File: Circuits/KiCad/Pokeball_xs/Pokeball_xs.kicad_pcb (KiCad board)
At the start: 2 copper layers, 30 x 30 mm, 21 parts, among them J1 Conn_01x05, J2 Conn_01x02, J3 Conn_01x06, U1 PIC12LF1571T-I_SN, U2 MCP1754ST-3302E_DB

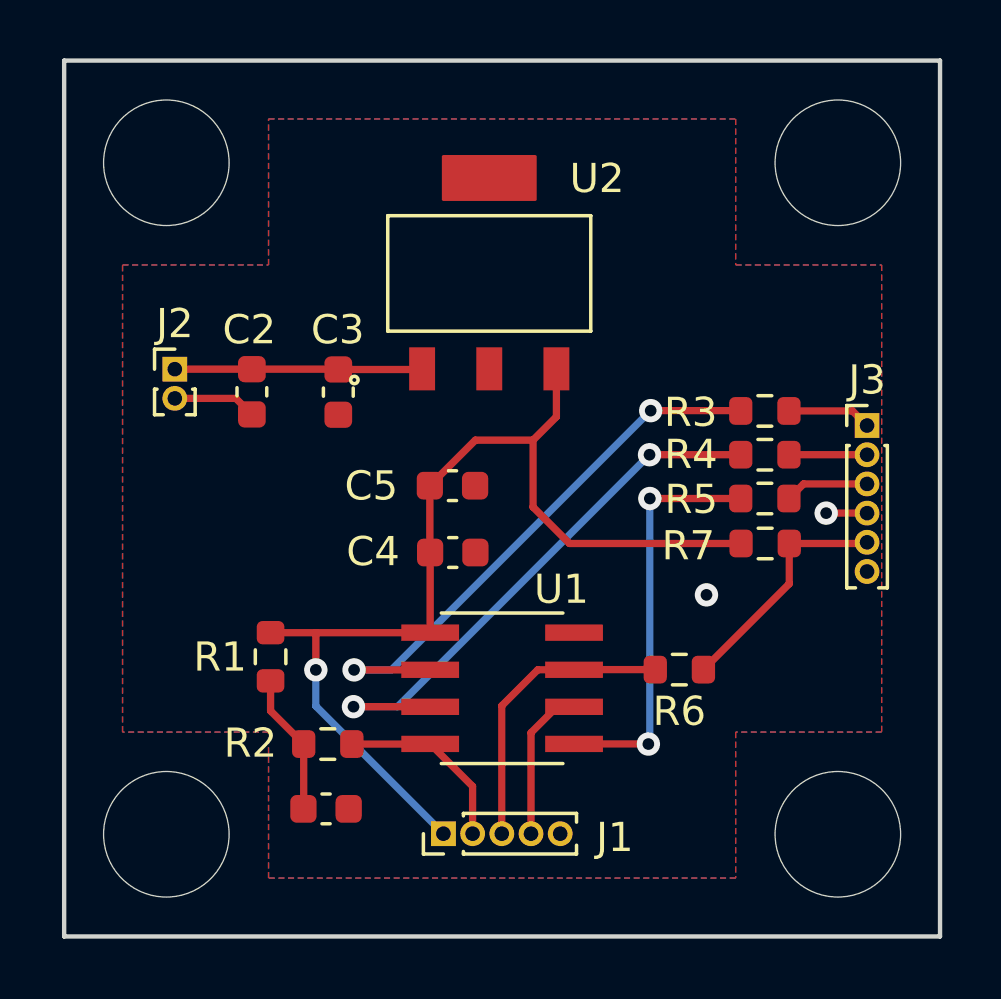
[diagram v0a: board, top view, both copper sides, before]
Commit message: v 0.0.0.1 - Include the charging circuit on the PCB
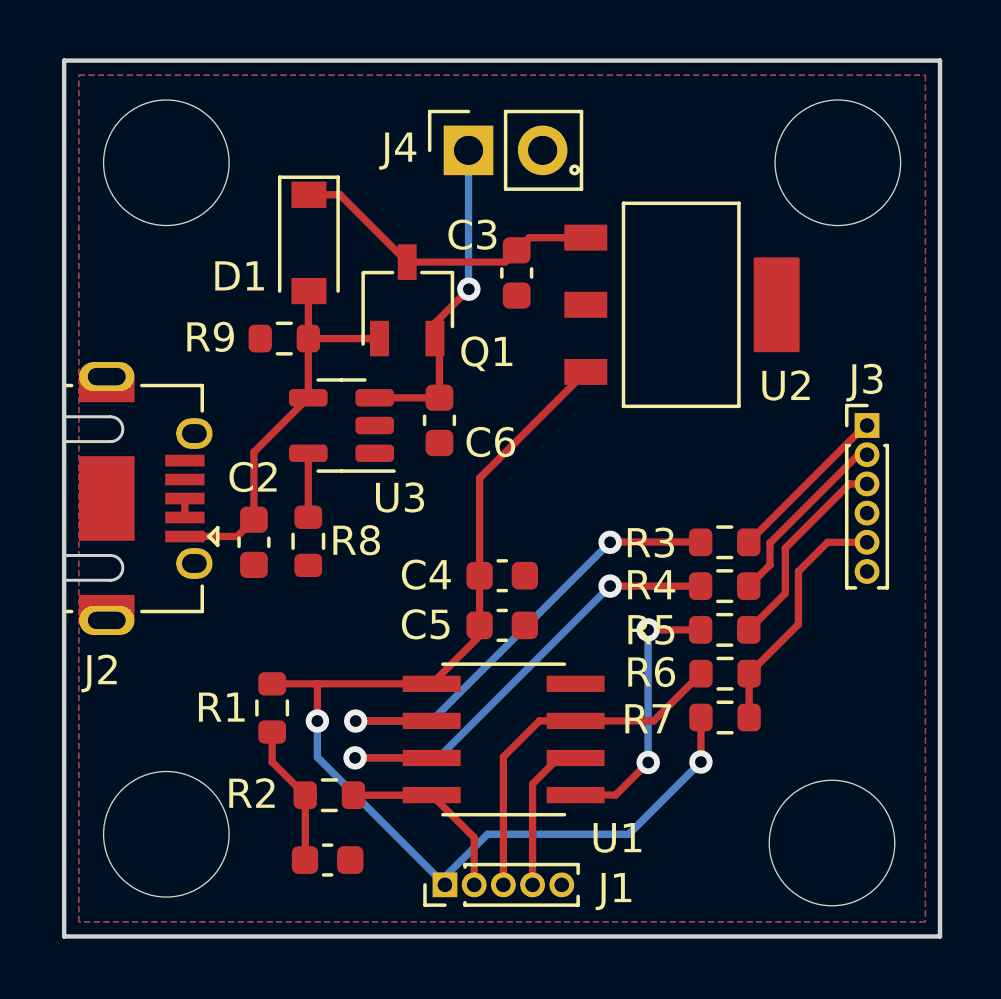
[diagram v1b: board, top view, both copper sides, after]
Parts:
- added C6: 4.7uF, Capacitor_SMD:C_0603_1608Metric, F.Cu at (137.9, 90.8)
- added D1: 40V 500mA, Diode_SMD:D_SOD-123, F.Cu at (133.4, 84.7)
- added J4: Battery, Connector_PinSocket_2.54mm:PinSocket_1x02_P2.54mm_Vertical, F.Cu at (138.8, 81.6)
- added Q1: 60V 170mA, Package_TO_SOT_SMD:TSOT-23, F.Cu at (136.7, 86.7)
- added R8: 10k, Resistor_SMD:R_0603_1608Metric, F.Cu at (133.4, 95.0)
- added R9: 10k, Resistor_SMD:R_0603_1608Metric, F.Cu at (132.5, 88.0)
- added U3: MCP73831-2-OT, Package_TO_SOT_SMD:SOT-23-5, F.Cu at (134.5, 91.0)
- C2: value 10uF 10v -> 4.7uF
- J2: value Conn_01x02 -> USB_B_Micro; footprint Connector_PinHeader_1.00mm:PinHeader_1x02_P1.00mm_Vertical -> Connector_USB:USB_Micro-AB_Molex_47590-0001
- moved C3 7.35 mm to (140.5, 85.8)
- moved U2 6.66 mm to (146.1, 86.9), turned to -90 degrees
- moved R7 6.12 mm to (147.6, 101.0)
- moved C2 5.16 mm to (131.5, 95.0)
- moved C5 5.08 mm to (140.0, 97.8)
- moved J2 5.01 mm to (126.5, 93.5), turned to -90 degrees
- moved R3 4.71 mm to (147.6, 95.0)
- moved R4 4.71 mm to (147.6, 96.5)
- moved R5 4.71 mm to (147.6, 98.0)
- moved C4 1.87 mm to (140.0, 96.1)
- moved C1 1.75 mm to (134.0, 105.9)
- moved J1 1.75 mm to (138.0, 106.7)
- moved R1 1.75 mm to (132.1, 100.7)
- moved R2 1.75 mm to (134.1, 103.7)
- moved U1 1.75 mm to (140.1, 101.8)
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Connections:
- C3 pad 1: Net-(C2-Pad1) -> Net-(C3-Pad1)
- J2 pad 2: GND -> Net-(J2-Pad2)
- U2 pad 1: Net-(C2-Pad1) -> Net-(C3-Pad1)
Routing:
- net Net-(C6-Pad1): track 0.00 -> 11.2 mm, vias 0 -> 1
- net Net-(C3-Pad1): track 0.00 -> 10.8 mm
- net Net-(C2-Pad1): track 8.48 -> 13.6 mm
- net PWM_3_BLUE: track 14.1 -> 9.29 mm
- net GND: track 4.27 -> 0.00 mm, vias 2 -> 0
- net Net-(J3-Pad3): track 2.88 -> 7.03 mm
- net Net-(J3-Pad2): track 2.68 -> 6.35 mm
- net Vcc: track 36.1 -> 39.2 mm, vias 1 -> 2
- net Net-(J3-Pad1): track 2.88 -> 5.71 mm
- net PWM_1_RED: track 19.5 -> 17.0 mm
- net PWM_2_GREEN: track 19.5 -> 16.9 mm
- net Net-(R8-Pad1): track 0.00 -> 2.19 mm
- net PGD: track 10.1 -> 12.3 mm
- net Net-(J2-Pad2): track 0.00 -> 0.65 mm

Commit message: v 0.0.0.2 - Testing the pwm output on the switch. Creation of the README.md.
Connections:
- net PWM_1_RED renamed PWM_4_RED
- net PWM_2_GREEN renamed PWM_3_GREEN
- net PWM_3_BLUE renamed PWM_1_BLUE
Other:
- outline, holes or cut-outs redrawn
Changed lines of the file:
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@@
   (net 6 "PGD")
   (net 7 "Net-(C2-Pad1)")
-  (net 8 "PWM_3_BLUE")
+  (net 8 "PWM_4_RED")
   (net 9 "Net-(J3-Pad1)")
-  (net 10 "PWM_2_GREEN")
+  (net 10 "PWM_3_GREEN")
   (net 11 "Net-(J3-Pad2)")
-  (net 12 "PWM_1_RED")
+  (net 12 "PWM_1_BLUE")
   (net 13 "Net-(J3-Pad3)")
   (net 14 "Net-(J3-Pad5)")
@@
       (net 4 "Vcc") (pinfunction "VDD") (pintype "power_in"))
     (pad "2" smd rect locked (at -2.4638 -0.635) (size 1.9812 0.5588) (layers "F.Cu" "F.Paste" "F.Mask")
-      (net 12 "PWM_1_RED") (pinfunction "RA5") (pintype "bidirectional"))
+      (net 8 "PWM_4_RED") (pinfunction "RA5") (pintype "bidirectional"))
     (pad "3" smd rect locked (at -2.4638 0.635) (size 1.9812 0.5588) (layers "F.Cu" "F.Paste" "F.Mask")
-      (net 10 "PWM_2_GREEN") (pinfunction "RA4") (pintype "bidirectional"))
+      (net 10 "PWM_3_GREEN") (pinfunction "RA4") (pintype "bidirectional"))
     (pad "4" smd rect locked (at -2.4638 1.905) (size 1.9812 0.5588) (layers "F.Cu" "F.Paste" "F.Mask")
       (net 1 "MCLR") (pinfunction "RA3/*MCLR/VPP") (pintype "bidirectional"))
     (pad "5" smd rect locked (at 2.4638 1.905) (size 1.9812 0.5588) (layers "F.Cu" "F.Paste" "F.Mask")
-      (net 8 "PWM_3_BLUE") (pinfunction "RA2") (pintype "bidirectional"))
+      (net 12 "PWM_1_BLUE") (pinfunction "RA2") (pintype "bidirectional"))
     (pad "6" smd rect locked (at 2.4638 0.635) (size 1.9812 0.5588) (layers "F.Cu" "F.Paste" "F.Mask")
       (net 5 "PGC") (pinfunction "RA1/ICSPCLK") (pintype "bidirectional"))
@@
       (net 9 "Net-(J3-Pad1)") (pintype "passive"))
     (pad "2" smd roundrect locked (at 0.825 0 180) (size 0.8 0.95) (layers "F.Cu" "F.Paste" "F.Mask") (roundrect_rratio 0.25)
-      (net 12 "PWM_1_RED") (pintype "passive"))
+      (net 8 "PWM_4_RED") (pintype "passive"))
     (model "${KISYS3DMOD}/Resistor_SMD.3dshapes/R_0603_1608Metric.wrl"
       (offset (xyz 0 0 0))
@@
       (net 11 "Net-(J3-Pad2)") (pintype "passive"))
     (pad "2" smd roundrect locked (at 0.825 0 180) (size 0.8 0.95) (layers "F.Cu" "F.Paste" "F.Mask") (roundrect_rratio 0.25)
-      (net 10 "PWM_2_GREEN") (pintype "passive"))
+      (net 10 "PWM_3_GREEN") (pintype "passive"))
     (model "${KISYS3DMOD}/Resistor_SMD.3dshapes/R_0603_1608Metric.wrl"
       (offset (xyz 0 0 0))
@@
       (net 13 "Net-(J3-Pad3)") (pintype "passive"))
     (pad "2" smd roundrect locked (at 0.825 0 180) (size 0.8 0.95) (layers "F.Cu" "F.Paste" "F.Mask") (roundrect_rratio 0.25)
-      (net 8 "PWM_3_BLUE") (pintype "passive"))
+      (net 12 "PWM_1_BLUE") (pintype "passive"))
     (model "${KISYS3DMOD}/Resistor_SMD.3dshapes/R_0603_1608Metric.wrl"
       (offset (xyz 0 0 0))
@@
   (gr_line (start 140 78.5) (end 140 108.5) (layer "Dwgs.User") (width 0.15))
   (gr_line (start 125 93.5) (end 155 93.5) (layer "Dwgs.User") (width 0.15))
-  (gr_line (start 125 78.5) (end 125 108.5) (layer "Edge.Cuts") (width 0.15))
+  (gr_line (start 125.01 89.75) (end 125 78.5) (layer "Edge.Cuts") (width 0.05))
+  (gr_line (start 125.01 97.25) (end 125 108.5) (layer "Edge.Cuts") (width 0.05))
   (gr_line (start 155 78.5) (end 125 78.5) (layer "Edge.Cuts") (width 0.15))
   (gr_line (start 155 108.5) (end 155 78.5) (layer "Edge.Cuts") (width 0.15))
@@
   (segment (start 131.5 91.9125) (end 133.3625 90.05) (width 0.25) (layer "F.Cu") (net 7))
   (segment (start 135.799229 88.021012) (end 135.79957 88.021353) (width 0.25) (layer "F.Cu") (net 7))
-  (segment (start 145.006003 102.540308) (end 143.888811 103.6575) (width 0.25) (layer "F.Cu") (net 8))
-  (segment (start 143.888811 103.6575) (end 142.5178 103.6575) (width 0.25) (layer "F.Cu") (net 8))
-  (segment (start 145 98) (end 146.8 98) (width 0.25) (layer "F.Cu") (net 8))
-  (via (at 145.006003 102.540308) (size 0.8) (drill 0.4) (layers "F.Cu" "B.Cu") (free) (net 8))
-  (via (at 145 98) (size 0.8) (drill 0.4) (layers "F.Cu" "B.Cu") (net 8))
-  (segment (start 145 102.534305) (end 145 98) (width 0.25) (layer "B.Cu") (net 8))
-  (segment (start 145.006003 102.540308) (end 145 102.534305) (width 0.25) (layer "B.Cu") (net 8))
+  (segment (start 143.71 94.99) (end 146.79 94.99) (width 0.25) (layer "F.Cu") (net 8))
+  (segment (start 134.984 101.1225) (end 137.5852 101.1225) (width 0.25) (layer "F.Cu") (net 8))
+  (segment (start 146.79 94.99) (end 146.8 95) (width 0.25) (layer "F.Cu") (net 8))
+  (segment (start 143.7 95) (end 143.71 94.99) (width 0.25) (layer "F.Cu") (net 8))
+  (segment (start 137.5852 101.1225) (end 137.5902 101.1175) (width 0.25) (layer "F.Cu") (net 8))
+  (via (at 143.7 95) (size 0.8) (drill 0.4) (layers "F.Cu" "B.Cu") (net 8))
+  (via (at 134.984 101.1225) (size 0.8) (drill 0.4) (layers "F.Cu" "B.Cu") (net 8))
+  (segment (start 134.984 101.1225) (end 137.5775 101.1225) (width 0.25) (layer "B.Cu") (net 8))
+  (segment (start 137.5775 101.1225) (end 143.7 95) (width 0.25) (layer "B.Cu") (net 8))
   (segment (start 148.45 94.99003) (end 152.44003 91) (width 0.25) (layer "F.Cu") (net 9))
   (segment (start 148.45 95) (end 148.45 94.99003) (width 0.25) (layer "F.Cu") (net 9))
@@
   (segment (start 152.2 92) (end 152.5 92) (width 0.25) (layer "F.Cu") (net 11))
   (segment (start 149.17452 95.77548) (end 149.17452 95.02548) (width 0.25) (layer "F.Cu") (net 11))
-  (segment (start 143.71 94.99) (end 146.79 94.99) (width 0.25) (layer "F.Cu") (net 12))
-  (segment (start 134.984 101.1225) (end 137.5852 101.1225) (width 0.25) (layer "F.Cu") (net 12))
-  (segment (start 146.79 94.99) (end 146.8 95) (width 0.25) (layer "F.Cu") (net 12))
-  (segment (start 143.7 95) (end 143.71 94.99) (width 0.25) (layer "F.Cu") (net 12))
-  (segment (start 137.5852 101.1225) (end 137.5902 101.1175) (width 0.25) (layer "F.Cu") (net 12))
-  (via (at 143.7 95) (size 0.8) (drill 0.4) (layers "F.Cu" "B.Cu") (net 12))
-  (via (at 134.984 101.1225) (size 0.8) (drill 0.4) (layers "F.Cu" "B.Cu") (net 12))
-  (segment (start 134.984 101.1225) (end 137.5775 101.1225) (width 0.25) (layer "B.Cu") (net 12))
-  (segment (start 137.5775 101.1225) (end 143.7 95) (width 0.25) (layer "B.Cu") (net 12))
+  (segment (start 145.006003 102.540308) (end 143.888811 103.6575) (width 0.25) (layer "F.Cu") (net 12))
+  (segment (start 143.888811 103.6575) (end 142.5178 103.6575) (width 0.25) (layer "F.Cu") (net 12))
+  (segment (start 145 98) (end 146.8 98) (width 0.25) (layer "F.Cu") (net 12))
+  (via (at 145.006003 102.540308) (size 0.8) (drill 0.4) (layers "F.Cu" "B.Cu") (free) (net 12))
+  (via (at 145 98) (size 0.8) (drill 0.4) (layers "F.Cu" "B.Cu") (net 12))
+  (segment (start 145 102.534305) (end 145 98) (width 0.25) (layer "B.Cu") (net 12))
+  (segment (start 145.006003 102.540308) (end 145 102.534305) (width 0.25) (layer "B.Cu") (net 12))
   (segment (start 149.7 95.2) (end 151.9 93) (width 0.25) (layer "F.Cu") (net 13))
   (segment (start 149.7 96.75) (end 149.7 95.2) (width 0.25) (layer "F.Cu") (net 13))
@@
     (connect_pads (clearance 0))
     (min_thickness 0.254)
-    (keepout (tracks not_allowed) (vias not_allowed) (pads not_allowed ) (copperpour not_allowed) (footprints allowed))
+    (keepout (tracks not_allowed) (vias not_allowed) (pads not_allowed) (copperpour not_allowed) (footprints allowed))
     (fill (thermal_gap 0.508) (thermal_bridge_width 0.508))
     (polygon
@@
     (connect_pads (clearance 0))
     (min_thickness 0.254)
-    (keepout (tracks not_allowed) (vias not_allowed) (pads not_allowed ) (copperpour not_allowed) (footprints allowed))
+    (keepout (tracks not_allowed) (vias not_allowed) (pads not_allowed) (copperpour not_allowed) (footprints allowed))
     (fill (thermal_gap 0.508) (thermal_bridge_width 0.508))
     (polygon

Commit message: v 0.0.0.3 - updates to the board and the mechanical system.
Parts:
- added G***: LOGO, Psyduck_xs:Psyduck_xs, F.Cu at (135.0, 81.0)
- moved R7 3.86 mm to (146.0, 104.5), turned to 90 degrees
- moved U2 1.30 mm to (145.0, 87.5)
- moved C3 1.00 mm to (139.5, 85.8)
- moved D1 0.67 mm to (134.0, 85.0)
- moved C1 0.61 mm to (134.5, 105.5)
- moved R2 0.54 mm to (134.5, 104.0)
- moved R1 0.51 mm to (132.5, 100.3)
- moved H3 0.36 mm to (151.5, 105.0)
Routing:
- net Vcc: track 39.2 -> 34.9 mm
- net Net-(J3-Pad5): track 8.52 -> 12.2 mm
- net Net-(C3-Pad1): track 10.8 -> 8.83 mm
- net Net-(C6-Pad1): track 11.2 -> 11.9 mm
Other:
- board text added: "+"
- board text added: "-"
- board text added: "B"
- board text added: "BTN"
- board text added: "G"
- board text added: "R"

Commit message: v 0.0.0.4 - submit rev 1 of the pokeball to pcbway.
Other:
- board text added: "JKnapp Rev1"
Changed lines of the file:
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@@
       (layerselection 0x00010fc_ffffffff)
       (disableapertmacros false)
-      (usegerberextensions false)
-      (usegerberattributes true)
+      (usegerberextensions true)
+      (usegerberattributes false)
       (usegerberadvancedattributes true)
-      (creategerberjobfile true)
+      (creategerberjobfile false)
       (svguseinch false)
       (svgprecision 6)
@@
       (outputformat 1)
       (mirror false)
-      (drillshape 1)
+      (drillshape 0)
       (scaleselection 1)
-      (outputdirectory "")
+      (outputdirectory "Pokeball_Kicad_Rev_1/")
     )
   )
@@
     (effects (font (size 0.5 0.5) (thickness 0.125)))
   )
+  (gr_text "JKnapp\nRev1" (at 144.5 81.5 90) (layer "F.SilkS")
+    (effects (font (size 0.5 0.5) (thickness 0.125)))
+  )

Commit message: v 0.0.0.8 - Board submitted to pcbway
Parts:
- removed R7: 4.7k, Resistor_SMD:R_0603_1608Metric
- added C7: 47uF, Capacitor_SMD:C_0603_1608Metric, F.Cu at (140.0, 95.0)
- added C8: 22uF, Capacitor_SMD:C_0603_1608Metric, F.Cu at (138.5, 95.0)
- C3: value 0.1uF 10v -> 0.1uF
- C4: value 100uF 10v -> 47uF
- C5: value 1uF 10v -> 1uF
- J1: footprint Connector_PinHeader_1.00mm:PinHeader_1x05_P1.00mm_Vertical -> Connector_PinHeader_2.00mm:PinHeader_1x05_P2.00mm_Vertical
- J2: footprint Connector_USB:USB_Micro-AB_Molex_47590-0001 -> Connector_USB:USB_Micro-B_Molex-105017-0001
- J3: footprint Connector_PinHeader_1.00mm:PinHeader_1x06_P1.00mm_Vertical -> Connector_PinHeader_2.00mm:PinHeader_1x06_P2.00mm_Vertical
- moved C5 3.21 mm to (141.5, 95.0), turned to -90 degrees
- moved C4 3.21 mm to (143.0, 95.0), turned to -90 degrees
- moved J3 2.55 mm to (152.0, 88.5)
- moved U1 2.25 mm to (140.1, 99.5)
- moved J1 2.17 mm to (136.0, 106.0)
- moved C2 2.03 mm to (131.4, 93.0)
- moved C1 2.00 mm to (134.5, 103.5)
- moved R2 2.00 mm to (134.5, 102.0)
- moved J2 1.04 mm to (127.5, 93.5)
- moved R1 0.69 mm to (132.0, 99.8)
- moved R3 0.50 mm to (147.6, 95.5)
- moved R4 0.50 mm to (147.6, 97.0)
- moved R5 0.50 mm to (147.6, 98.5)
- moved R6 0.50 mm to (147.6, 100.0)
- moved R8 0.32 mm to (133.4, 94.6)
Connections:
- net PWM_1_BLUE renamed PWM_3_BLUE
- net PWM_3_GREEN renamed PWM_2_GREEN
- net PWM_4_RED renamed PWM_1_RED
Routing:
- net Net-(J3-Pad5): track 12.2 -> 4.99 mm
- net Vcc: track 34.9 -> 29.0 mm, vias 2 -> 1
- net Net-(J3-Pad1): track 5.71 -> 8.98 mm
- net Net-(C2-Pad1): track 13.6 -> 11.5 mm
- net PGC: track 5.30 -> 7.12 mm
- net Net-(J3-Pad2): track 6.35 -> 7.97 mm
- net MCLR: track 6.08 -> 7.55 mm
- net PWM_3_BLUE: track 9.29 -> 7.91 mm
- net PWM_2_GREEN: track 16.9 -> 15.7 mm
- net Net-(C1-Pad1): track 4.86 -> 3.73 mm
- net PWM_1_RED: track 17.0 -> 15.9 mm
- net PGD: track 12.3 -> 13.3 mm
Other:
- outline, holes or cut-outs redrawn
- board text added: "."
- board text added: "JKnapp Rev2"
- board text removed: "JKnapp Rev1"
